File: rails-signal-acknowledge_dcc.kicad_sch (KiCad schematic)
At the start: 4 parts, among them Q501 S8050

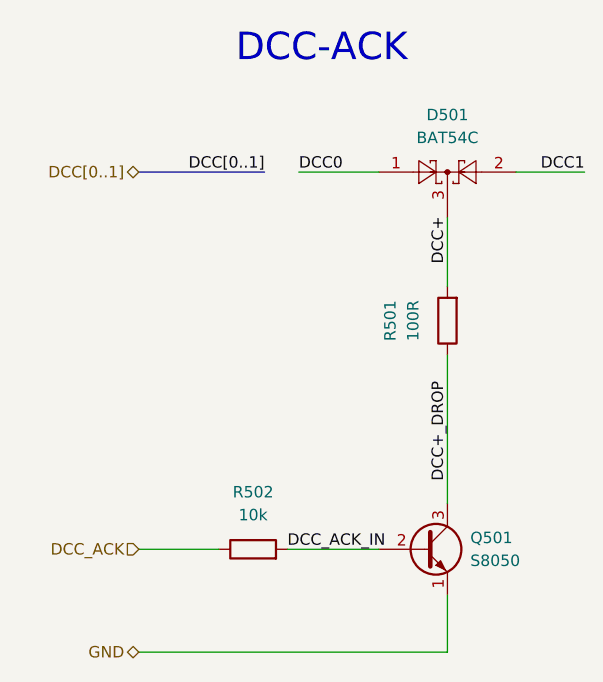
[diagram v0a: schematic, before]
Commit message: Fix - Remove ERC error, refresh annotation
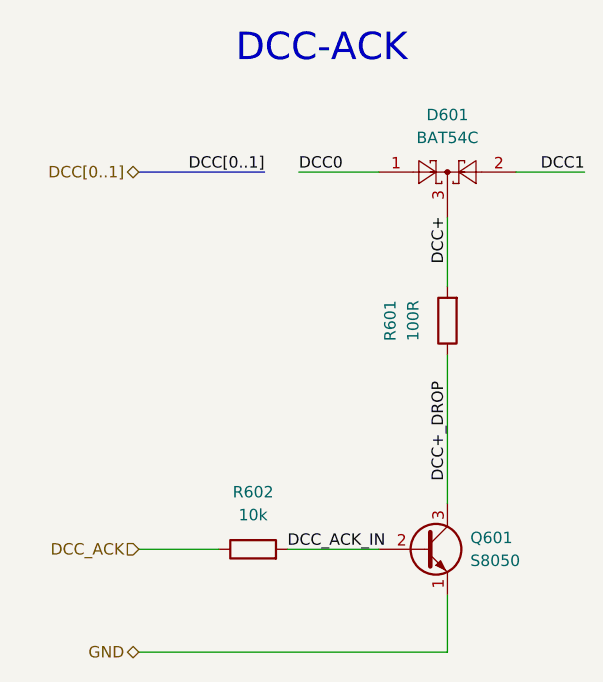
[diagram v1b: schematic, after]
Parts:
- renumbered D501 to D601, Q501 to Q601, R501 to R601, R502 to R602
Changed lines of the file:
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@@
 		(on_board yes)
 		(dnp no)
-		(property "Reference" "R501"
+		(property "Reference" "R601"
 			(at 62.23 53.34 90)
 			(effects
@@
 			(project "xDuinoRails-Fortuna-M"
 				(path "/fb33ec4e-6596-45d2-a121-8d3475acd69a/c9229de7-1ed3-435d-9b11-33fa2e05ec65/deaf1b68-8bb1-4a22-bf5f-eab4be33579f"
-					(reference "R501")
+					(reference "R601")
 					(unit 1)
 				)
@@
 		(dnp no)
 		(fields_autoplaced yes)
-		(property "Reference" "D501"
+		(property "Reference" "D601"
 			(at 68.58 30.48 0)
 			(effects
@@
 			(project "xDuinoRails-Fortuna-M"
 				(path "/fb33ec4e-6596-45d2-a121-8d3475acd69a/c9229de7-1ed3-435d-9b11-33fa2e05ec65/deaf1b68-8bb1-4a22-bf5f-eab4be33579f"
-					(reference "D501")
+					(reference "D601")
 					(unit 1)
 				)
@@
 		(on_board yes)
 		(dnp no)
-		(property "Reference" "R502"
+		(property "Reference" "R602"
 			(at 46.99 72.39 90)
 			(effects
@@
 			(project "xDuinoRails-Fortuna-M"
 				(path "/fb33ec4e-6596-45d2-a121-8d3475acd69a/c9229de7-1ed3-435d-9b11-33fa2e05ec65/deaf1b68-8bb1-4a22-bf5f-eab4be33579f"
-					(reference "R502")
+					(reference "R602")
 					(unit 1)
 				)
@@
 		(on_board yes)
 		(dnp no)
-		(property "Reference" "Q501"
+		(property "Reference" "Q601"
 			(at 71.12 77.47 0)
 			(effects
@@
 			(project "xDuinoRails-Fortuna-M"
 				(path "/fb33ec4e-6596-45d2-a121-8d3475acd69a/c9229de7-1ed3-435d-9b11-33fa2e05ec65/deaf1b68-8bb1-4a22-bf5f-eab4be33579f"
-					(reference "Q501")
+					(reference "Q601")
 					(unit 1)
 				)

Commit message: Fix - revert to working model
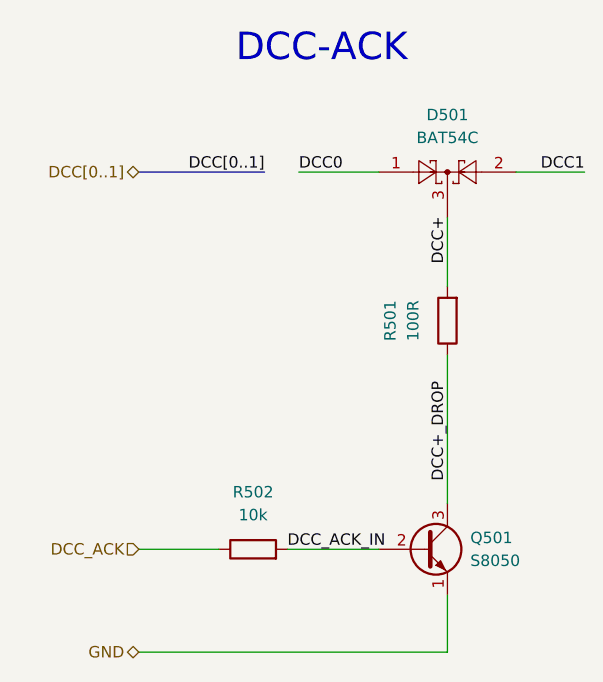
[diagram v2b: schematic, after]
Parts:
- renumbered D601 to D501, Q601 to Q501, R601 to R501, R602 to R502
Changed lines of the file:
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@@
 		(on_board yes)
 		(dnp no)
-		(property "Reference" "R601"
+		(property "Reference" "R501"
 			(at 62.23 53.34 90)
 			(effects
@@
 			(project "xDuinoRails-Fortuna-M"
 				(path "/fb33ec4e-6596-45d2-a121-8d3475acd69a/c9229de7-1ed3-435d-9b11-33fa2e05ec65/deaf1b68-8bb1-4a22-bf5f-eab4be33579f"
-					(reference "R601")
+					(reference "R501")
 					(unit 1)
 				)
@@
 		(dnp no)
 		(fields_autoplaced yes)
-		(property "Reference" "D601"
+		(property "Reference" "D501"
 			(at 68.58 30.48 0)
 			(effects
@@
 			(project "xDuinoRails-Fortuna-M"
 				(path "/fb33ec4e-6596-45d2-a121-8d3475acd69a/c9229de7-1ed3-435d-9b11-33fa2e05ec65/deaf1b68-8bb1-4a22-bf5f-eab4be33579f"
-					(reference "D601")
+					(reference "D501")
 					(unit 1)
 				)
@@
 		(on_board yes)
 		(dnp no)
-		(property "Reference" "R602"
+		(property "Reference" "R502"
 			(at 46.99 72.39 90)
 			(effects
@@
 			(project "xDuinoRails-Fortuna-M"
 				(path "/fb33ec4e-6596-45d2-a121-8d3475acd69a/c9229de7-1ed3-435d-9b11-33fa2e05ec65/deaf1b68-8bb1-4a22-bf5f-eab4be33579f"
-					(reference "R602")
+					(reference "R502")
 					(unit 1)
 				)
@@
 		(on_board yes)
 		(dnp no)
-		(property "Reference" "Q601"
+		(property "Reference" "Q501"
 			(at 71.12 77.47 0)
 			(effects
@@
 			(project "xDuinoRails-Fortuna-M"
 				(path "/fb33ec4e-6596-45d2-a121-8d3475acd69a/c9229de7-1ed3-435d-9b11-33fa2e05ec65/deaf1b68-8bb1-4a22-bf5f-eab4be33579f"
-					(reference "Q601")
+					(reference "Q501")
 					(unit 1)
 				)
